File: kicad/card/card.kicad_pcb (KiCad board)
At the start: 2 copper layers, 30 x 34 mm, 34 parts, among them SW1 USB_BOOT, SW2 RESET, U1 RP2350A, U2 TLV70030_SOT23-5, U3 W25Q128, Y1 12MHz

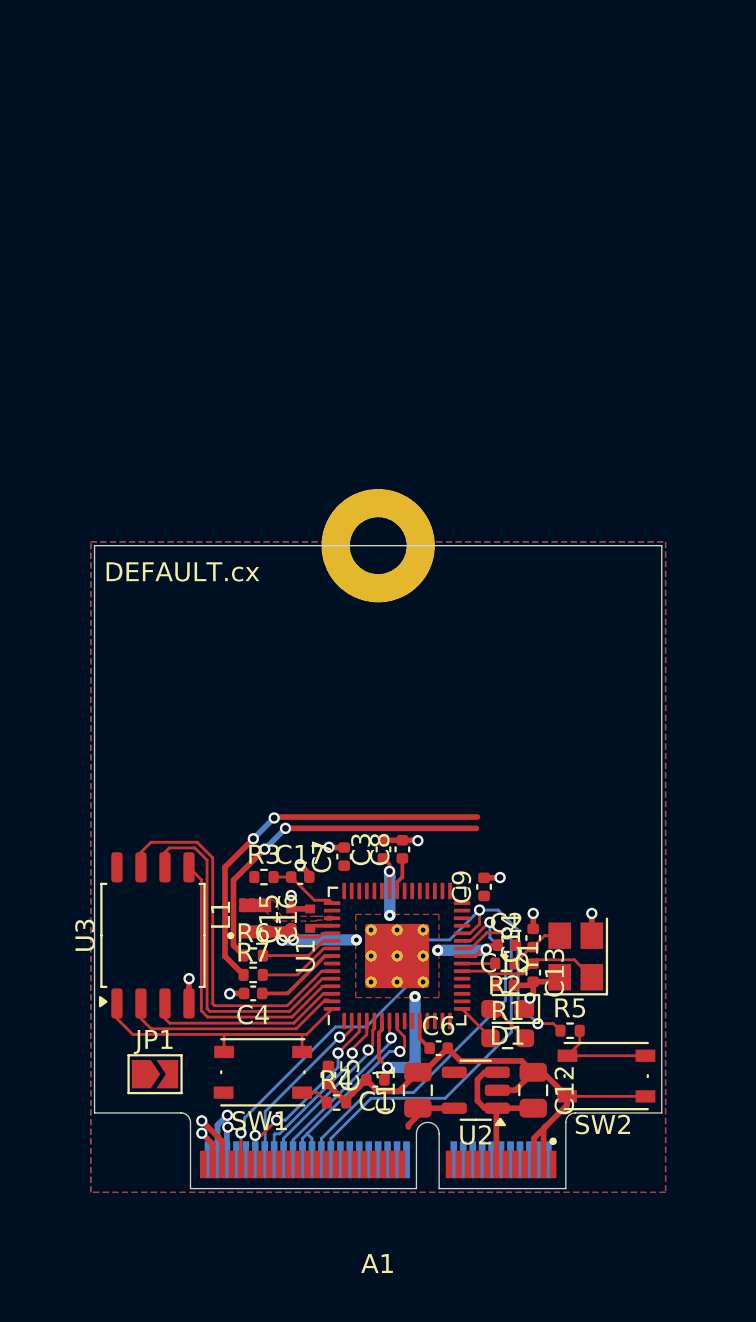
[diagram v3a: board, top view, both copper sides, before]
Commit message: routed, 5V alt and IMU stub
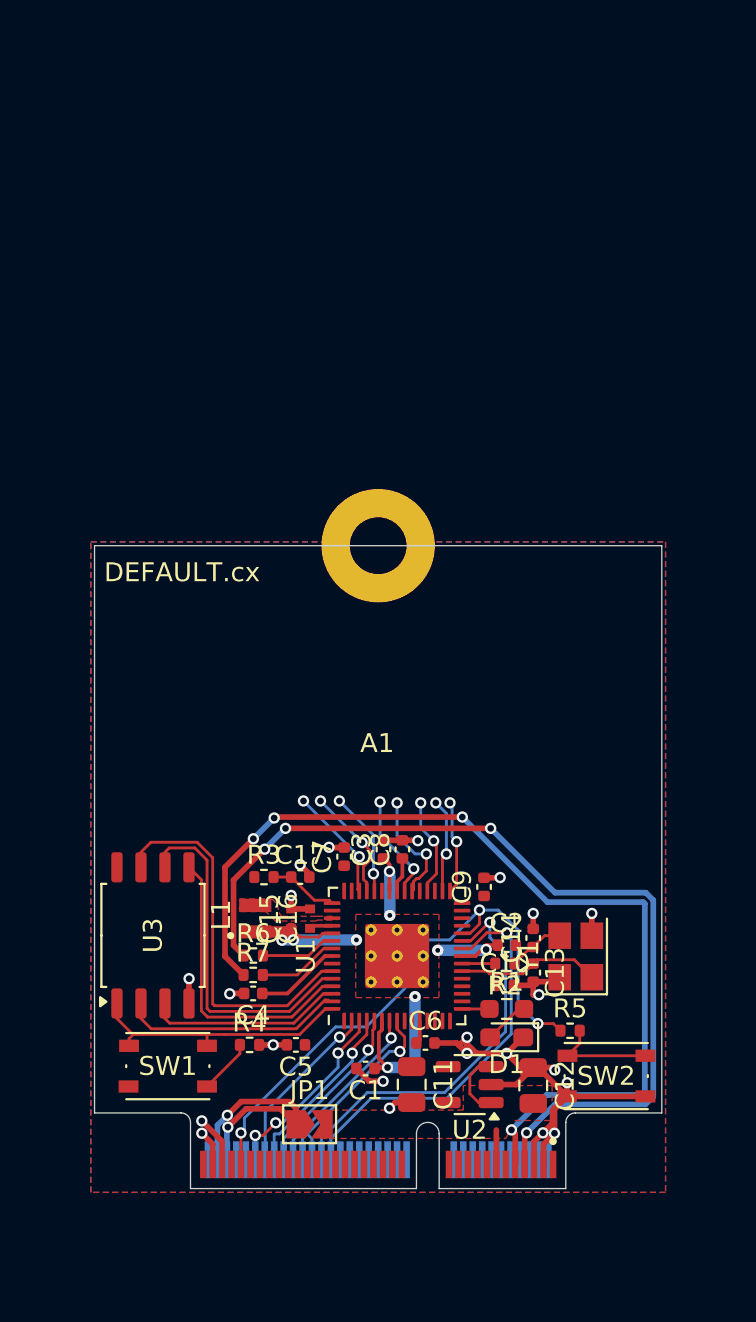
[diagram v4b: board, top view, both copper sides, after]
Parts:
- SW1: value USB_BOOT -> BOOT
- moved JP1 8.59 mm to (96.4, 128.8)
- moved R4 5.52 mm to (93.2, 124.6)
- moved SW1 5.04 mm to (88.9, 125.7)
- moved C5 2.34 mm to (95.7, 124.6), turned to 180 degrees
- moved R1 1.55 mm to (106.8, 122.7)
- moved D1 1.50 mm to (106.8, 124.2)
- moved C1 0.79 mm to (99.3, 125.8)
- moved C6 0.75 mm to (102.5, 124.5)
- moved C11 0.44 mm to (101.8, 126.7), turned to -90 degrees
- moved U2 0.44 mm to (104.8, 126.7)
- moved C12 0.25 mm to (108.2, 126.8)
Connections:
- A1 pad 13: Net-(JP1-B) -> +5V
- A1 pad 18: unconnected-(A1-GND-Pad18) -> GND
- A1 pad 2: Net-(U1-GPIO27_ADC1) -> Net-(A1-3v3-Pad2)
- A1 pad 38: Net-(A1-TP85) -> unconnected-(A1-TP85-Pad38)
- A1 pad 4: Net-(U1-GPIO27_ADC1) -> Net-(A1-3v3-Pad2)
- A1 pad 46: Net-(A1-TP86) -> unconnected-(A1-TP86-Pad46)
- A1 pad 68: Net-(JP1-A) -> +5V
- A1 pad 70: Net-(JP1-A) -> +5V
- A1 pad 72: Net-(JP1-A) -> +5V
- C12 pad 2: Net-(JP1-B) -> +5V
- JP1 pad 1: Net-(JP1-A) -> +5V
- JP1 pad 2: Net-(JP1-B) -> +5V
- U1 pad 41: Net-(U1-GPIO27_ADC1) -> unconnected-(U1-GPIO27_ADC1-Pad41)
- U1 pad 42: Net-(A1-TP86) -> unconnected-(U1-GPIO28_ADC2-Pad42)
- U1 pad 43: Net-(A1-TP85) -> unconnected-(U1-GPIO29_ADC3-Pad43)
- U2 pad 1: Net-(JP1-B) -> +5V
- U2 pad 3: Net-(JP1-B) -> +5V
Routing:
- net Net-(A1-USB_DP): track 20.6 -> 51.1 mm, vias 2 -> 4
- net Net-(A1-USB_DM): track 18.2 -> 48.7 mm, vias 2 -> 4
- net +5V: track 0.00 -> 19.0 mm, vias 0 -> 2
- net Net-(JP1-B): track 8.44 -> 0.00 mm
- net unconnected-(U1-GPIO28_ADC2-Pad42): track 0.00 -> 6.09 mm, vias 0 -> 2
- net unconnected-(U1-GPIO29_ADC3-Pad43): track 0.00 -> 6.05 mm, vias 0 -> 2
- net unconnected-(U1-GPIO24-Pad36): track 0.00 -> 6.03 mm, vias 0 -> 2
- net unconnected-(U1-GPIO25-Pad37): track 0.00 -> 5.65 mm, vias 0 -> 2
- net unconnected-(U1-GPIO27_ADC1-Pad41): track 0.00 -> 5.53 mm, vias 0 -> 2
- net unconnected-(U1-GPIO22-Pad34): track 0.00 -> 5.22 mm, vias 0 -> 2
- net unconnected-(U1-GPIO20-Pad32): track 0.00 -> 4.98 mm, vias 0 -> 2
- net unconnected-(U1-GPIO19-Pad31): track 0.00 -> 4.95 mm, vias 0 -> 2
- net GND: track 47.0 -> 51.8 mm, vias 12 -> 22
- net Net-(JP1-A): track 4.31 -> 0.00 mm, vias 2 -> 0
- net +3V3: track 12.4 -> 8.81 mm
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- added copper zone on F.Cu, net +5V
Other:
- board text added: "DEFAULT.cx"
- board text added: "defa1337"

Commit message: added 2mm headers and fabrication files
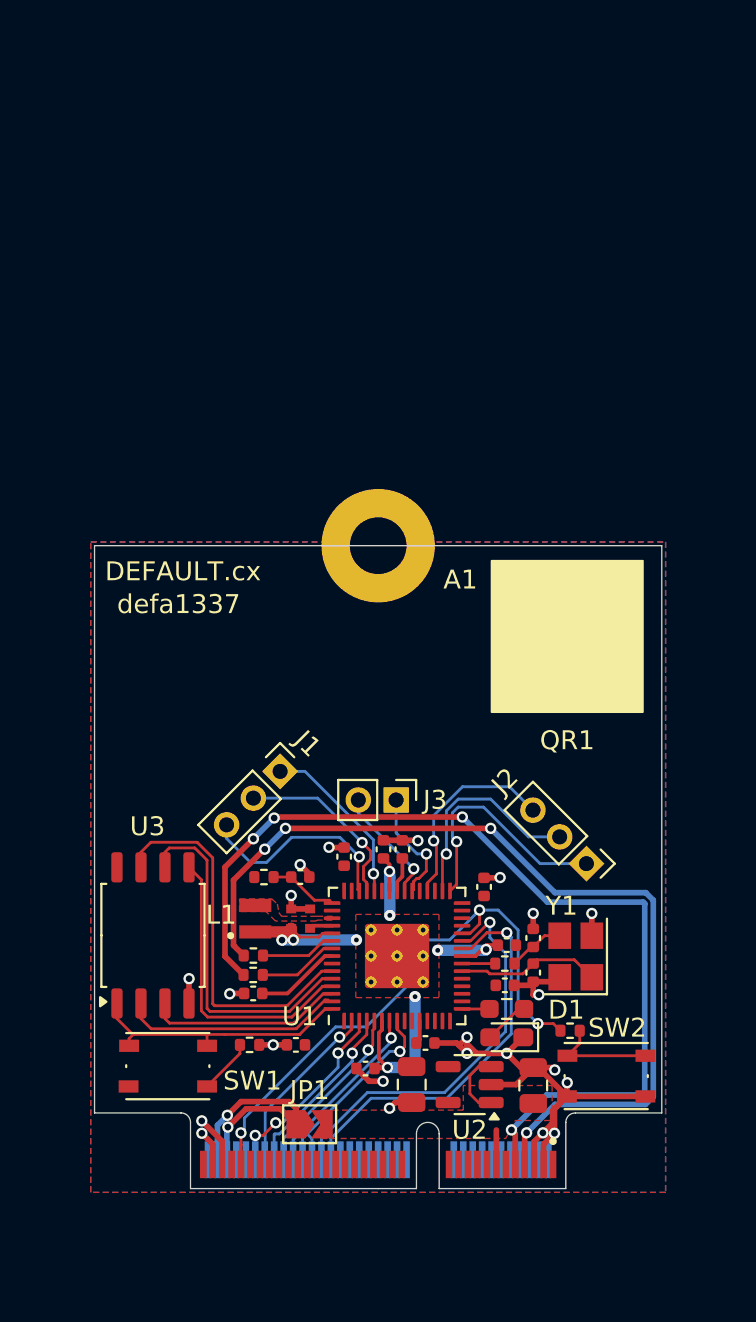
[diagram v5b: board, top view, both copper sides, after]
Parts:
- added J1: ADC, Connector_PinHeader_2.00mm:PinHeader_1x03_P2.00mm_Vertical, F.Cu at (94.8, 110.1)
- added J2: SPI, Connector_PinHeader_2.00mm:PinHeader_1x03_P2.00mm_Vertical, F.Cu at (111.0, 115.0)
- added J3: I2C, Connector_PinHeader_2.00mm:PinHeader_1x02_P2.00mm_Vertical, F.Cu at (101.0, 111.7)
- added QR1: ~, DEFAULT:QR_8x8, F.Cu at (110.0, 103.0)
- SW1: value BOOT -> USB_BOOT
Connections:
- net /~{USB_BOOT} renamed /~{BOOT}
- U1 pad 31: unconnected-(U1-GPIO19-Pad31) -> Net-(J2-Pin_1)
- U1 pad 32: unconnected-(U1-GPIO20-Pad32) -> Net-(J2-Pin_2)
- U1 pad 34: unconnected-(U1-GPIO22-Pad34) -> Net-(J2-Pin_3)
- U1 pad 36: unconnected-(U1-GPIO24-Pad36) -> Net-(J3-Pin_1)
- U1 pad 37: unconnected-(U1-GPIO25-Pad37) -> Net-(J3-Pin_2)
- U1 pad 41: unconnected-(U1-GPIO27_ADC1-Pad41) -> Net-(J1-Pin_1)
- U1 pad 42: unconnected-(U1-GPIO28_ADC2-Pad42) -> Net-(J1-Pin_2)
- U1 pad 43: unconnected-(U1-GPIO29_ADC3-Pad43) -> Net-(J1-Pin_3)
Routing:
- net Net-(J2-Pin_1): track 0.00 -> 12.8 mm, vias 0 -> 1
- net Net-(J2-Pin_2): track 0.00 -> 11.4 mm, vias 0 -> 1
- net Net-(J1-Pin_3): track 0.00 -> 11.1 mm, vias 0 -> 1
- net Net-(J2-Pin_3): track 0.00 -> 10.7 mm, vias 0 -> 1
- net Net-(J1-Pin_2): track 0.00 -> 9.70 mm, vias 0 -> 1
- net Net-(J1-Pin_1): track 0.00 -> 9.16 mm, vias 0 -> 1
- net Net-(J3-Pin_2): track 0.00 -> 6.23 mm, vias 0 -> 1
- net Net-(J3-Pin_1): track 0.00 -> 6.14 mm, vias 0 -> 1
- net unconnected-(U1-GPIO28_ADC2-Pad42): track 6.09 -> 0.00 mm, vias 2 -> 0
- net unconnected-(U1-GPIO29_ADC3-Pad43): track 6.05 -> 0.00 mm, vias 2 -> 0
- net unconnected-(U1-GPIO24-Pad36): track 6.03 -> 0.00 mm, vias 2 -> 0
- net unconnected-(U1-GPIO25-Pad37): track 5.65 -> 0.00 mm, vias 2 -> 0
- net unconnected-(U1-GPIO27_ADC1-Pad41): track 5.53 -> 0.00 mm, vias 2 -> 0
- net unconnected-(U1-GPIO22-Pad34): track 5.22 -> 0.00 mm, vias 2 -> 0
- net unconnected-(U1-GPIO20-Pad32): track 4.98 -> 0.00 mm, vias 2 -> 0
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
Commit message: BNO08x IMU
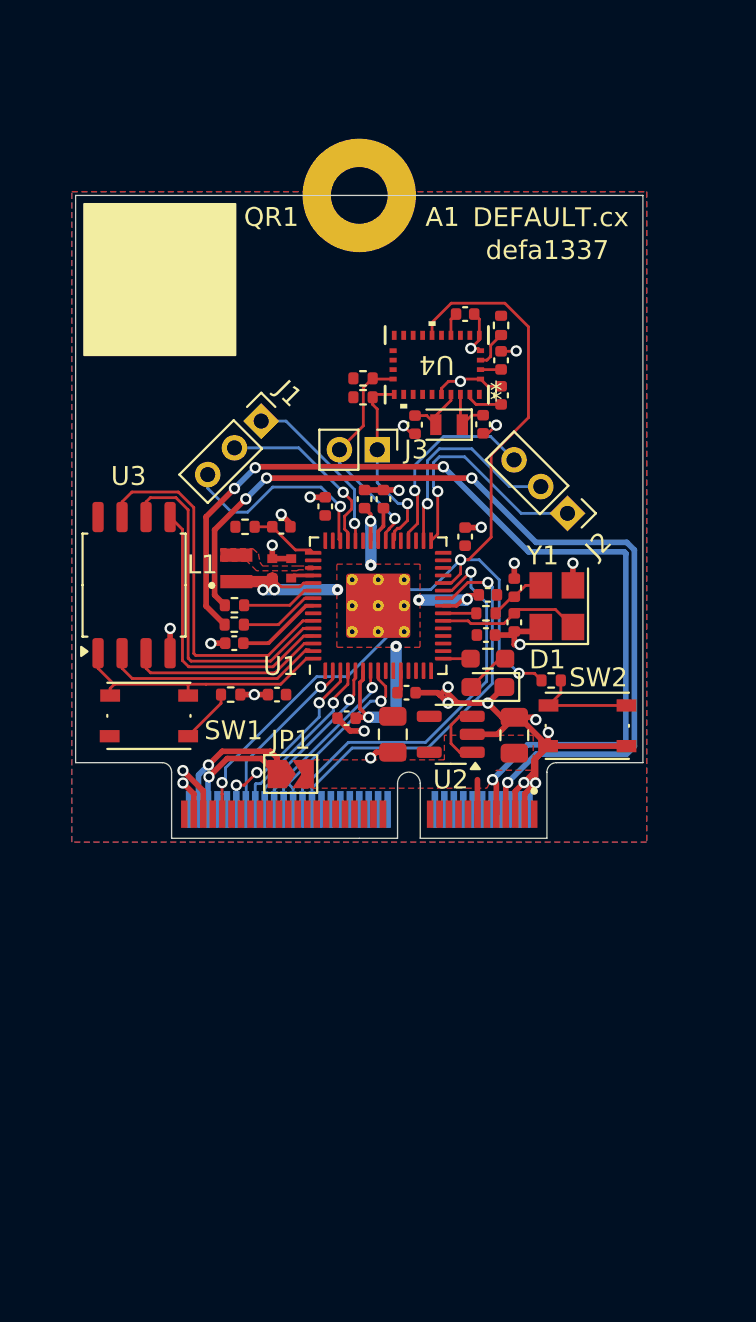
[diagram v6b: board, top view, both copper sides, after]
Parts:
- added C18: 22pF, Capacitor_SMD:C_0402_1005Metric, F.Cu at (102.0, 91.8)
- added C19: 22pF, Capacitor_SMD:C_0402_1005Metric, F.Cu at (105.5, 91.8)
- added C20: 0.1uF, Capacitor_SMD:C_0402_1005Metric, F.Cu at (106.5, 90.2)
- added C21: 0.1uF, Capacitor_SMD:C_0402_1005Metric, F.Cu at (106.5, 88.4)
- added C22: 0.1uF, Capacitor_SMD:C_0402_1005Metric, F.Cu at (104.6, 85.9)
- added R10: 2.2K, Resistor_SMD:R_0402_1005Metric, F.Cu at (99.2, 90.3)
- added R8: 10K, Resistor_SMD:R_0402_1005Metric, F.Cu at (106.5, 86.5)
- added R9: 2.2K, Resistor_SMD:R_0402_1005Metric, F.Cu at (99.2, 89.3)
- added U4: BNO086, DEFAULT:QFN28_BNO086_CEV, F.Cu at (103.1, 88.6)
- added Y2: 32.768kHz, Crystal:Crystal_SMD_2012-2Pin_2.0x1.2mm, F.Cu at (103.8, 91.8)
- moved QR1 28.6 mm to (88.5, 84.1)
- moved C10 18.6 mm to (105.7, 102.9)
- moved C11 18.6 mm to (100.8, 108.2)
- moved C12 18.6 mm to (107.2, 108.2)
- moved C13 18.6 mm to (107.2, 102.3)
- moved C2 18.6 mm to (105.8, 100.8)
- moved C3 18.6 mm to (99.3, 95.7)
- moved C6 18.6 mm to (101.5, 106.0)
- moved C8 18.6 mm to (100.3, 95.7)
- moved C9 18.6 mm to (104.6, 97.7)
- moved D1 18.6 mm to (105.8, 105.7)
- moved J3 18.6 mm to (100.0, 93.1)
- moved JP1 18.6 mm to (95.4, 110.3)
- moved R1 18.6 mm to (105.8, 104.2)
- moved R6 18.6 mm to (92.4, 101.3)
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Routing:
- net Net-(A1-XIO_A): track 31.5 -> 52.2 mm
- net GND: track 51.8 -> 60.8 mm, vias 22 -> 27
- net Net-(J3-Pin_2): track 6.23 -> 11.8 mm
- net Net-(J3-Pin_1): track 6.14 -> 10.2 mm
- net Net-(U4-XOUT32/CLKSEL1): track 0.00 -> 3.23 mm
- net +3V3: track 8.81 -> 11.9 mm
- net Net-(U4-XIN32): track 0.00 -> 2.95 mm
- net Net-(U4-BOOTN): track 0.00 -> 1.98 mm
- net Net-(U4-CAP): track 0.00 -> 1.24 mm

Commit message: 0.1" Breadboard header
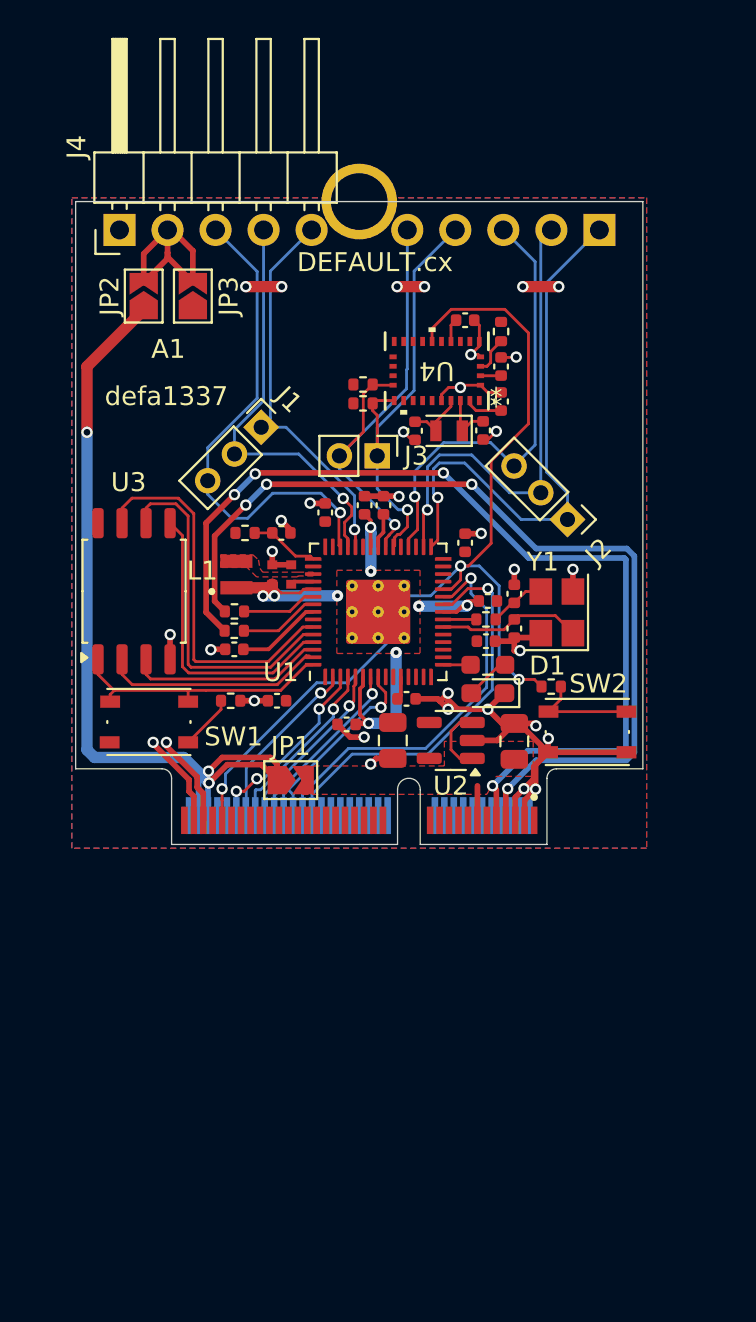
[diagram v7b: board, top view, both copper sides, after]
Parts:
- added J4: Conn_01x05_Pin, Connector_PinHeader_2.54mm:PinHeader_1x05_P2.54mm_Horizontal, F.Cu at (86.3, 81.5)
- added J5: Conn_01x05_Pin, Connector_PinHeader_2.54mm:PinHeader_1x05_P2.54mm_Horizontal, B.Cu at (111.7, 81.5)
- added JP2: Alt 5V, Jumper:SolderJumper-2_P1.3mm_Open_TrianglePad1.0x1.5mm, F.Cu at (87.6, 85.0)
- added JP3: Alt 3V3, Jumper:SolderJumper-2_P1.3mm_Open_TrianglePad1.0x1.5mm, F.Cu at (90.2, 85.0)
- QR1: moved to B.Cu
- moved QR1 3.20 mm to (88.5, 87.3), turned to 180 degrees
- moved A1 0.33 mm to (99.0, 114.0)
- moved C1 0.33 mm to (98.3, 107.7)
- moved C10 0.33 mm to (105.7, 103.2)
- moved C11 0.33 mm to (100.8, 108.5)
- moved C12 0.33 mm to (107.2, 108.5)
- moved C13 0.33 mm to (107.2, 102.6)
- moved C14 0.33 mm to (107.2, 100.7)
- moved C17 0.33 mm to (94.9, 97.5)
- moved C18 0.33 mm to (102.0, 92.1)
- moved C19 0.33 mm to (105.5, 92.1)
- moved C2 0.33 mm to (105.8, 101.1)
- moved C20 0.33 mm to (106.5, 90.6)
- moved C21 0.33 mm to (106.5, 88.7)
- moved C3 0.33 mm to (99.3, 96.1)
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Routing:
- net +5V: track 19.0 -> 50.7 mm, vias 2 -> 3
- net Net-(J2-Pin_1): track 12.8 -> 29.8 mm
- net Net-(J1-Pin_3): track 11.1 -> 26.4 mm
- net Net-(J2-Pin_2): track 11.4 -> 25.5 mm
- net Net-(J3-Pin_1): track 10.2 -> 23.9 mm
- net Net-(J2-Pin_3): track 10.7 -> 24.3 mm
- net Net-(J3-Pin_2): track 11.8 -> 25.3 mm
- net Net-(J1-Pin_2): track 9.70 -> 22.2 mm
- net Net-(J4-Pin_2): track 0.00 -> 12.2 mm
- net Net-(J1-Pin_1): track 9.16 -> 20.7 mm
- net GND: track 60.8 -> 71.4 mm, vias 27 -> 33
